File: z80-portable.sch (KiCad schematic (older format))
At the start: 45 parts, among them J1 Conn_01x40, J2 Barrel_Jack_MountingPin, J3 Conn_01x03, J4 Conn_01x06, J5 Conn_01x14, SW1 SW_Push, U1 74HC157, U10 DS1233-5+, U11 L7805, U2 74HC137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

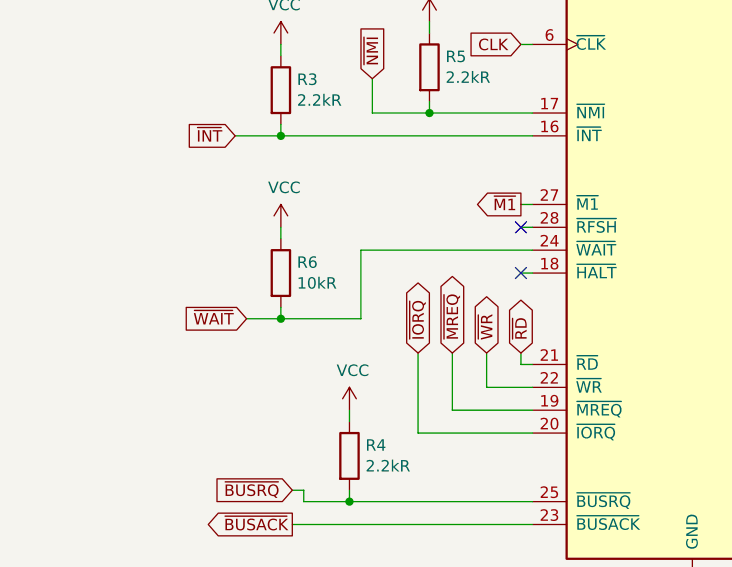
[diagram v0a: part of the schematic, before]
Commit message: Fixed a few minor mistakes, no need to reorder PCB
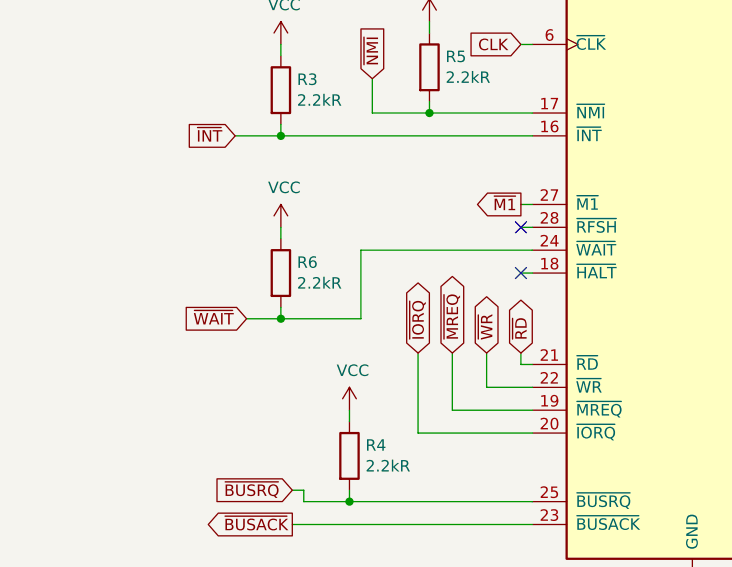
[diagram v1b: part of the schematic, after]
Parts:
- R6: value 10kR -> 2.2kR
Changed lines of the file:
@@
 P 1450 9100
 F 0 "R6" H 1520 9146 50  0000 L CNN
-F 1 "10kR" H 1520 9055 50  0000 L CNN
+F 1 "2.2kR" H 1520 9055 50  0000 L CNN
 F 2 "Resistor_THT:R_Axial_DIN0204_L3.6mm_D1.6mm_P5.08mm_Horizontal" V 1380 9100 50  0001 C CNN
 F 3 "~" H 1450 9100 50  0001 C CNN
